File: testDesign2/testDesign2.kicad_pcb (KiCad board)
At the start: 2 copper layers, 39 x 26 mm, 31 parts, among them SW1 SW_Push, U1 CC2640R2FRSM, Y1 32.768kHz, Y2 24MHz

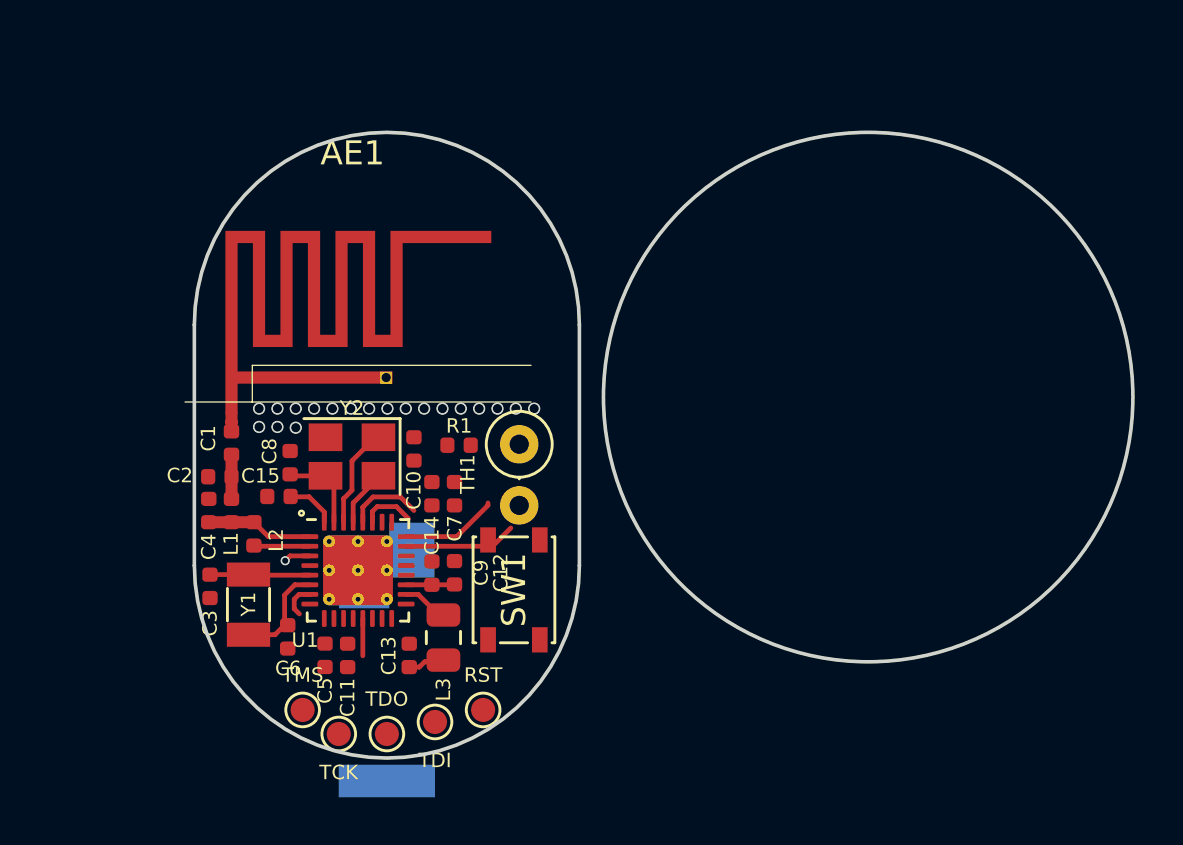
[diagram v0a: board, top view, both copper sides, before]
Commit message: Enclosure and PCB needs to be a CIRCLE
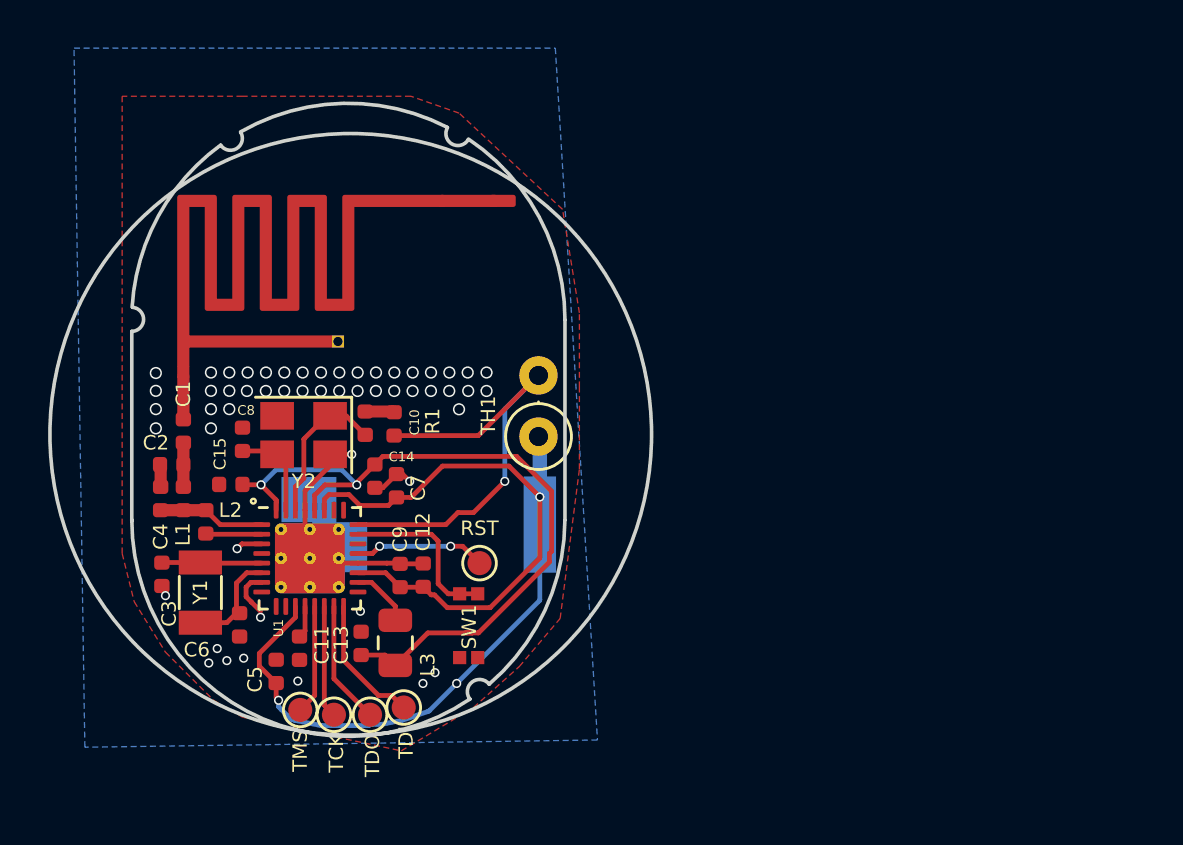
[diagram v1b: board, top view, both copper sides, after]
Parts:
- SW1: footprint Button_Switch_SMD:SW_SPST_PTS810 -> testDesign:Switch_EVP-BB4A9B000
- moved RST 6.10 mm to (111.8, 116.4)
- moved BT1 3.11 mm to (105.4, 114.8), turned to 180 degrees
- moved R1 2.84 mm to (108.3, 110.6), turned to 90 degrees
- moved AE1 2.50 mm to (99.3, 108.2)
- moved C14 2.48 mm to (107.5, 112.8), turned to 270 degrees
- moved C7 2.43 mm to (108.4, 113.2)
- moved SW1 2.40 mm to (111.4, 119.0), turned to 270 degrees
- moved C10 2.29 mm to (107.1, 110.6)
- moved C8 2.20 mm to (102.0, 111.3)
- moved Y2 2.20 mm to (104.5, 111.1)
- moved C5 2.14 mm to (103.4, 120.9), turned to 90 degrees
- moved C1 2.06 mm to (99.5, 110.9)
- moved C13 2.06 mm to (106.9, 119.7)
- moved C15 2.06 mm to (101.5, 113.1)
- moved C2 2.06 mm to (99.1, 112.3)
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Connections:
- U1 pad 23: ADC0 -> Button
- U1 pad 24: Button -> ADC0
- U1 pad 33: (no net) -> GND
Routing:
- net VDDS: track 3.97 -> 47.5 mm, vias 0 -> 3
- net VDDR: track 6.69 -> 31.5 mm, vias 0 -> 2
- net ADC0: track 4.66 -> 19.0 mm, vias 0 -> 1
- net GND: track 4.37 -> 16.5 mm, vias 20 -> 53
- net Net-(TP7-Pad1): track 0.00 -> 5.55 mm
- net Net-(TP11-Pad1): track 0.00 -> 5.46 mm, vias 0 -> 2
- net Net-(TP6-Pad1): track 0.00 -> 5.12 mm
- net Net-(TP5-Pad1): track 0.00 -> 4.67 mm
- net Button: track 4.04 -> 7.04 mm
- net Net-(TP4-Pad1): track 1.55 -> 4.55 mm
- net Net-(C10-Pad1): track 4.07 -> 6.72 mm
- net Net-(C11-Pad1): track 0.00 -> 1.35 mm
- net DCDC_SW: track 1.49 -> 2.55 mm
- net Net-(AE1-Pad1): track 0.78 -> 1.78 mm
- net Net-(C8-Pad1): track 3.25 -> 4.05 mm
- added copper zone on B.Cu, net GND
- added copper zone on F.Cu, net GND
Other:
- board size 39 x 26 mm -> 25 x 26.3 mm

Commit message: Think PCB design is finished. Need to do last checkthrough.
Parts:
- C12, C13, C9: footprint Capacitor_SMD:C_0402_1005Metric -> Capacitor_SMD:C_0603_1608Metric
- TH1: footprint Resistor_THT:R_Axial_DIN0207_L6.3mm_D2.5mm_P2.54mm_Vertical -> Resistor_THT:R_Axial_DIN0204_L3.6mm_D1.6mm_P1.90mm_Vertical; moved to B.Cu
- moved C6 80.8 mm to (49.8, 57.2), turned to 90 degrees
- moved C5 79.7 mm to (54.3, 58.1), turned to 270 degrees
- moved C12 79.5 mm to (59.5, 55.1), turned to 270 degrees
- moved C1 79.3 mm to (51.0, 48.2)
- moved C2 79.2 mm to (50.5, 49.7)
- moved SW1 79.2 mm to (64.4, 55.3)
- moved L1 79.1 mm to (51.0, 51.2)
- moved TDI 79.0 mm to (62.0, 58.7), turned to 180 degrees
- moved U1 79.0 mm to (56.0, 54.1)
- moved C11 79.0 mm to (55.3, 58.1)
- moved RST 78.9 mm to (65.1, 52.8), turned to 180 degrees
- moved TDO 78.9 mm to (60.4, 59.3), turned to 180 degrees
- moved C3 78.8 mm to (49.8, 55.1)
- moved C14 78.8 mm to (59.1, 50.7), turned to 90 degrees
- moved C10 78.6 mm to (58.7, 48.6)
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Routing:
- net ADC0: track 19.0 -> 11.3 mm
- net GND: track 16.5 -> 11.4 mm, vias 53 -> 116
- net VDDR: track 31.5 -> 28.2 mm, vias 2 -> 4
- net Net-(C6-Pad1): track 4.04 -> 6.46 mm
- net Net-(TP11-Pad1): track 5.46 -> 7.56 mm, vias 2 -> 0
- net DCDC_SW: track 2.55 -> 4.30 mm
- net Net-(AE1-Pad1): track 1.78 -> 0.73 mm
- net Net-(C3-Pad1): track 3.59 -> 4.57 mm
- net Net-(TP4-Pad1): track 4.55 -> 3.97 mm
- net VDDS: track 47.5 -> 47.1 mm, vias 3 -> 1
- net Button: track 7.04 -> 7.37 mm, vias 0 -> 2
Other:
- board size 25 x 26.3 mm -> 24 x 24 mm
- net class Default: clearance 0.2 -> 0.1524; trace_width 0.25 -> 0.1524; via_dia 0.8 -> 0.381; via_drill 0.4 -> 0.254
- rule pad_to_mask_clearance: 0.051 -> 0
- rule trace_clearance: 0.2 -> 0.1524

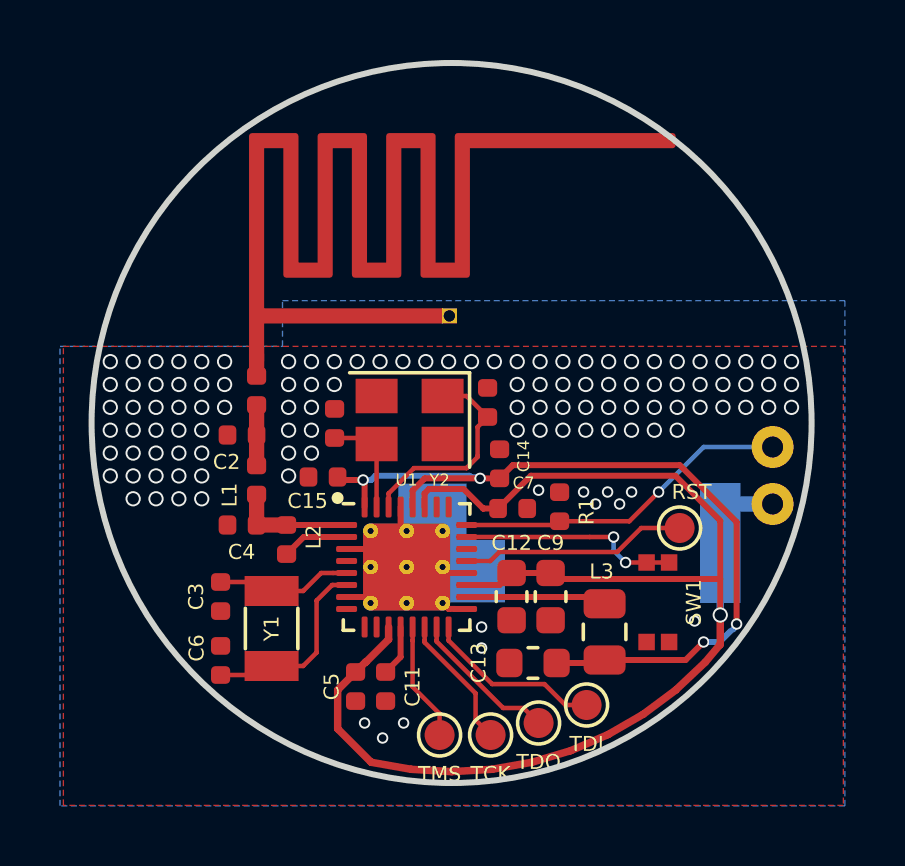
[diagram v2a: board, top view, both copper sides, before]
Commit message: Added mounts to PCB and started enclosure.
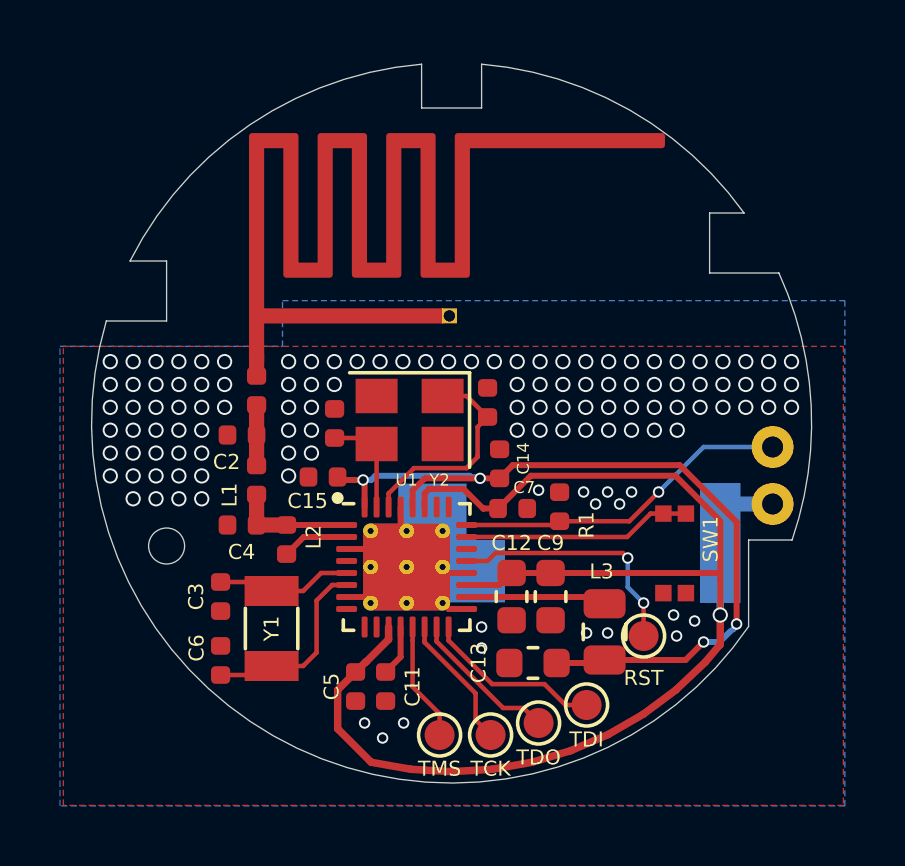
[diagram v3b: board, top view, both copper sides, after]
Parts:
- added H1: MountingHole, testDesign:MountingHole_1.2mm_M1, F.Cu at (48.0, 53.4)
- moved RST 3.79 mm to (63.9, 56.4)
- moved SW1 1.72 mm to (64.9, 53.6)
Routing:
- net Net-(TP11-Pad1): track 7.56 -> 8.37 mm, vias 0 -> 2
- net Button: track 7.37 -> 7.67 mm, vias 2 -> 0
- net GND: vias 116 -> 120
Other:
- outline, holes or cut-outs redrawn
